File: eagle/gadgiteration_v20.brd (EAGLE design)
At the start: 76.3 x 63.5 mm, 50 parts, among them IC1 ATMEGA328P, J1 2.1MMJACK, X1 16.00MHz

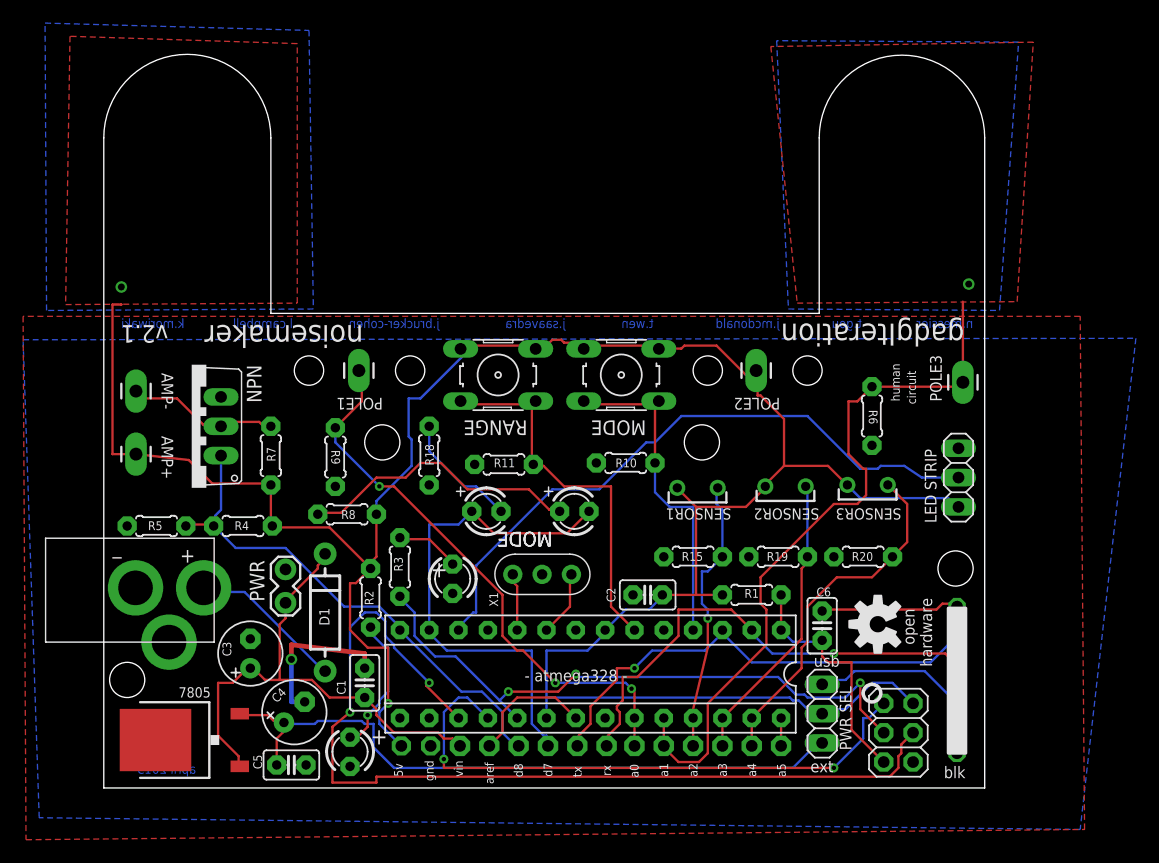
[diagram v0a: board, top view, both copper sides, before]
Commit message: added v21 files, including readme and eagle files
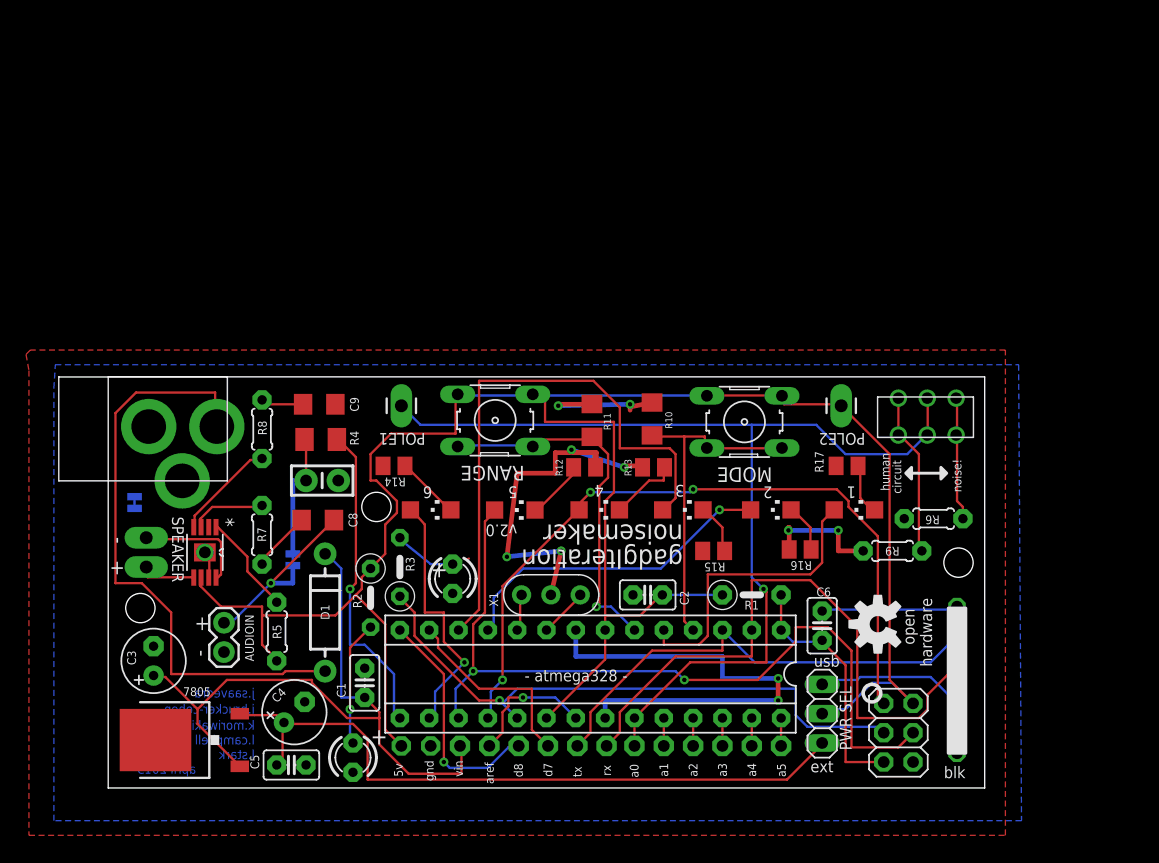
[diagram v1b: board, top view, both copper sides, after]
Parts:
- removed AMP+, AMP-, POLE3: M01PTH_LONGPAD, SparkFun-Connectors:1X01_LONGPAD
- removed LED7, LED8: (no value), adafruit:LED3MM
- removed LED_STRIP: (no value), pinhead:1X03
- removed NPN: (no value), transistor:TO220V
- removed PH1, PH2, PH3: M9960_11B, photo-elements:M9960
- removed PWR: (no value), SparkFun-Connectors:1X02_LOCK
- removed R18, R19, R20: (no value), adafruit:0204/5
- added AUDIOIN: IN, SparkFun:1X02
- added C7: 0.1uF, SparkFun-Capacitors:CAP-PTH-SMALL-KIT
- added C8, C9: 1uF, SparkFun:1206
- added LED1, LED2, LED3, LED4, LED5, LED6: (no value), led:CHIPLED_1206
- added R12, R13, R14, R16, R17: (no value), resistor:M0805
- added SJ1, SJ2: SOLDERJUMPERTRACE, SparkFun-Passives:SJ_2S-TRACE
- added SPEAKER: OUT, SparkFun-Connectors:1X02_LONGPADS
- added U$1: (no value), jms_SparkFun-Electromechanical:EG1271
- added U2: TPA2005D1DGNRQ1, Texas Instruments_By_element14_Batch_1:SOP65P490X110-9N
- IC1: value ATMEGA328P -> ATMEGA168P
- R1: device adafruit:0204/5 -> rcl-ez:0207/5V
- R10, R11: device adafruit:0204/5 -> jms:R1206
- R15: device adafruit:0204/5 -> resistor:M0805
- R2, R3: device adafruit:0204/5 -> minimidi:0207/5V
- R4: value (none) -> 3.3k; device adafruit:0204/5 -> adafruit:M1206
- R5: value (none) -> 10K
- R7, R8: value (none) -> 150K
- moved R9 48.9 mm to (68.1, 20.6), turned to 180 degrees
- moved J1 14.0 mm to (0.25, 31.2)
- moved R5 13.9 mm to (14.7, 13.6), turned to 270 degrees
- moved MODE 11.4 mm to (55.2, 31.8)
- moved R8 10.4 mm to (13.5, 31.1), turned to 270 degrees
- moved R6 10.4 mm to (71.6, 23.4), turned to 0 degrees
- moved R4 10.1 mm to (18.5, 30.2), turned to 180 degrees
- moved R11 8.52 mm to (42.0, 31.9), turned to 270 degrees
- moved C3 8.41 mm to (4.06, 11.0)
- moved POLE2 7.97 mm to (63.6, 33.1)
- moved R7 6.90 mm to (13.5, 22.0), turned to 90 degrees
- moved POLE1 4.78 mm to (25.5, 33.1)
- moved R10 4.44 mm to (47.2, 32.0), turned to 270 degrees
- moved RANGE 3.95 mm to (33.7, 31.9)
- moved X1 1.93 mm to (38.5, 16.8)
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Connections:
- removed net +9V: PWR.2
- removed net SPKR_OUT: AMP-.1, NPN.2, R7.1
- new net IN+: AUDIOIN.1, C8.1, SJ1.2
- new net IN+AMP: R7.2, U2.3
- new net IN+_: C7.2, R4.2, SJ1.1
- new net IN-AMP: R8.2, U2.4
- new net N$10: LED6.C, R13.1
- new net N$11: LED4.C, R14.1
- new net N$12: LED3.C, R15.1
- new net N$13: LED2.C, R16.1
- new net N$14: LED1.C, R17.1
- new net N$18: SPEAKER.1, U2.5
- new net N$19: SPEAKER.2, U2.8
- new net N$5: LED5.C, R12.1
- new net N$8: R6.2, U$1.P$5, U$1.P$6
- new net N$9: R9.1, U$1.P$1, U$1.P$2
- new net SDN*: R5.1, U2.1
- net +5V: now also R5.2, U2.6; no longer AMP+.1, LED_STRIP.1, PH1.1, PH2.1, PH3.1, R4.2, R7.2, R8.1
- net ANALOG0: now also U$1.P$3, U$1.P$4; no longer R9.1
- net ANALOG1: no longer POLE3.1, R6.2
- net ANALOG2: no longer PH1.2, R15.2
- net ANALOG3: no longer PH2.2, R19.2
- net ANALOG4: no longer PH3.2, R20.2
- net DIGITAL10: now also LED4.A
- net DIGITAL3: now also LED1.A
- net DIGITAL5: now also LED2.A
- net DIGITAL6: now also LED3.A; no longer LED_STRIP.2
- net DIGITAL7: no longer LED7.A, LED8.K
- net DIGITAL8: no longer NPN.1, R4.1, R5.2
- net DIGITAL9: now also R4.1
- net GND: now also AUDIOIN.2, C7.1, C9.1, R12.2, R13.2, R14.2, R15.2, R16.2, R17.2, SJ2.1, SJ2.2, U2.7, U2.9; no longer LED_STRIP.3, NPN.3, R15.1, R18.2, R19.1, R20.1, R5.1
- net MISO: now also LED6.A
- net MOSI: now also LED5.A
- net N$6: now also C8.2, R7.1; no longer LED7.K, R18.1
- net N$7: now also C9.2, R8.1; no longer LED8.A, R8.2
- net VIN: no longer PWR.1
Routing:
- net GND: track 13.8 -> 101.4 mm, vias 1 -> 11
- net ANALOG1: track 63.4 -> 2.41 mm, vias 1 -> 0
- net ANALOG0: track 49.1 -> 88.4 mm, vias 3 -> 1
- net N$17: track 13.5 -> 51.8 mm
- net +5V: track 216.3 -> 182.6 mm, vias 2 -> 0
- net DIGITAL5: track 0.00 -> 28.7 mm, vias 0 -> 1
- net ANALOG4: track 30.7 -> 2.41 mm
- net DIGITAL9: track 0.00 -> 27.9 mm, vias 0 -> 1
- net DIGITAL7: track 43.8 -> 17.0 mm
- net DIGITAL3: track 0.00 -> 26.1 mm
- net DIGITAL8: track 44.4 -> 20.5 mm, vias 0 -> 1
- net ANALOG3: track 25.7 -> 2.41 mm
- net DIGITAL10: track 0.00 -> 22.5 mm, vias 0 -> 1
- net ANALOG2: track 24.0 -> 2.41 mm, vias 1 -> 0
- net N$7: track 24.6 -> 3.93 mm
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- removed copper zone on layer 1, net +5V
- removed copper zone on layer 16, net +5V
- removed copper zone on layer 1, net ANALOG1
- removed copper zone on layer 16, net ANALOG1
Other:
- board size 76.3 x 63.5 mm -> 75.9 x 35.6 mm
- board text added: "-"
- board text added: "1"
- board text added: "2"
- board text added: "3"
- board text added: "4"
- board text added: "5"
- board text added: "6"
- board text added: "l.stark"
- board text added: "noise!"
- board text added: "v2.0"
- board text removed: "LED STRIP"
- board text removed: "SENSOR1"
- board text removed: "SENSOR2"
- board text removed: "SENSOR3"
- board text removed: "_"
- board text removed: "j.mcdonald"
- board text removed: "n.messier"
- board text removed: "t.gou"
- board text removed: "t.wen"
- board text removed: "v2.1"
